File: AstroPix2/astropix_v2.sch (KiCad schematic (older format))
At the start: 41 parts, among them J1 pcie_con, J10 SPI_right, J2 VDD_JP, J3 Vtemp1, J4 SFOut, J5 sample_clock_out, J6 HV_in_external, J7 Conn_01x03, J8 Conn_01x03, J9 SPI_left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

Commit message: PCB: Updated Astropix2 schematic
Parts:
- removed H3, H4: MountingHole, MountingHole:MountingHole_3.2mm_M3, symbol Mechanical:MountingHole
- removed J7: Conn_01x03, Connector_PinHeader_2.54mm:PinHeader_1x03_P2.54mm_Vertical, symbol Connector_Generic:Conn_01x03
- removed U1, U3: OPA320, Package_TO_SOT_SMD:SOT-23-5, symbol Amplifier_Operational:OPA340NA
- added FID1, FID2: Fiducial, Fiducial:Fiducial_1mm_Mask2mm, symbol Mechanical:Fiducial
- added R11, R12: 1k, Resistor_SMD:R_0603_1608Metric, symbol Device:R
- added R13, R14: NC, Resistor_SMD:R_0603_1608Metric, symbol Device:R
- added U1: TLV333, Package_TO_SOT_SMD:SOT-23-6, symbol Amplifier_Operational:ADA4841-1YRJ
- added U3: OPA320S, Package_TO_SOT_SMD:SOT-23-6, symbol Amplifier_Operational:ADA4841-1YRJ
- C3, C4: value .1uF -> 1nF; footprint Capacitor_SMD:C_0603_1608Metric -> Capacitor_SMD:C_1210_3225Metric
- C5, C6: footprint Capacitor_SMD:C_0603_1608Metric -> Capacitor_SMD:C_1210_3225Metric
- J1: value pcie_con -> pcie_GECCO; symbol astropix:pcie_con -> astropix:pcie_GECCO
- R1, R10: value 1k -> 0
- R2: value 22 -> 47
- renumbered C7 to Cvdd1, C8 to Cvdd2, C13 to Cvdd3, C9 to Cvdda1, C10 to Cvdda2, C11 to Cvdda3
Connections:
- net GND: now also U4.B3 (gnda!), R14.2, U1.2 (V-), U3.2 (V-)
- net Inj: now also J1.A28 (C3_1); no longer J1.A36 (C5_1)
- net SFOut: now also U3.3 (+)
- net VDD: now also R13.1
- net VDDA: now also U4.B37 (vdda_temp), U1.5 (~PD), U1.6 (V+), U3.5 (~PD), U3.6 (V+); no longer R8.2
- net Vtemp1: now also U1.3 (+)
- net hold: now also J1.B23 (FMC_LA18_CC_N); no longer J1.B21 (FMC_LA20_N)
- net interrupt: now also J1.B21 (FMC_LA20_N); no longer J1.B18 (FMC_LA22_P)
- net res_n: now also J1.B22 (FMC_LA18_CC_P); no longer J1.B19 (FMC_LA22_N)
- net sample_clock_N: now also J1.B19 (FMC_LA22_N), R14.1; no longer J1.B17 (FMC_LA24_N)
- net sample_clock_P: now also J1.B18 (FMC_LA22_P), R13.2; no longer J1.B16 (FMC_LA24_P)
- net sample_clock_se_N: now also J1.B17 (FMC_LA24_N)
- net sample_clock_se_P: now also J1.B16 (FMC_LA24_P), R8.2
- net sample_clock_se_in: now also R8.1
- net sc_out: now also J5.1 (In)
- net spi_left_clk: now also J1.A16 (FMC_LA23_P)
- net spi_left_csn: now also J1.A17 (FMC_LA23_N)
- net spi_left_miso0: now also J1.A19 (FMC_LA21_N)
- net spi_left_miso1: now also J1.A18 (FMC_LA21_P), J9.3 (Pin_3); no longer J9.1 (Pin_1)
- net spi_left_mosi: now also J1.A20 (FMC_LA19_P), J9.1 (Pin_1); no longer J9.3 (Pin_3)
- net spi_right_clk: now also J10.1 (Pin_1); no longer J10.4 (Pin_4)
- net spi_right_csn: now also J10.4 (Pin_4); no longer J10.5 (Pin_5)
- net spi_right_miso0: now also J10.3 (Pin_3); no longer J10.2 (Pin_2)
- net spi_right_miso1: now also J10.2 (Pin_2); no longer J10.1 (Pin_1)
- net spi_right_mosi: now also J10.5 (Pin_5); no longer J10.3 (Pin_3)
- net sr_sout: now also J1.A23 (FMC_LA17_CC_N); no longer J5.1 (In)
- net suba: now also R12.2; no longer C3.2, C5.2, R1.1, R10.1, U4.B1 (sub), U4.B2 (subdpads)
- net at R6.2: now also U3.1, U3.4 (-)
- net at R2.2: now also U1.1, U1.4 (-)
- new net: R1.1, R10.1, R11.1, R12.1
- new net subd: C3.2, C5.2, R11.2, U4.B1 (sub), U4.B2 (subdpads)
- no-connect marks 58 -> 63
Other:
- note added: "100 Ohm Term + opt. Failsafe"
- note added: "PCB compatible to:\nOPA320S SOT-23-6\nOPA320 SOT-23-5 \n"
- moved on the sheet: C1, C12, C2, C3, C4, C5, C6, J10, J3, J4, J5, J8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

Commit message: PCB: Updated AstroPix2 Schematic
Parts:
- removed J2: VDD_JP, Connector_PinHeader_2.54mm:PinHeader_1x03_P2.54mm_Vertical, symbol Connector_Generic:Conn_01x03
- removed R10: 0, Resistor_SMD:R_0603_1608Metric, symbol Device:R
- added JP1: VDD_JP, Connector_PinHeader_2.54mm:PinHeader_1x03_P2.54mm_Vertical, symbol Jumper:Jumper_3_Bridged12
- added Logo1: KIT_logo, astropix:logo, symbol astropix:KIT_logo
- added R15: 1k, Resistor_SMD:R_0603_1608Metric, symbol Device:R
- added R16: 2k, Resistor_SMD:R_0603_1608Metric, symbol Device:R
- J8: value Conn_01x03 -> VBias
- R1: footprint Resistor_SMD:R_0603_1608Metric -> Resistor_SMD:R_1206_3216Metric
- R9: value 10k -> 680
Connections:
- net GND: now also U4.B17 (sr_RB), R15.2; no longer R9.2
- net POW4_in: now also JP1.3 (B)
- net VDD: now also JP1.2 (C)
- net VDD18_in: now also JP1.1 (A)
- net Vtemp1: now also R9.2; no longer U1.3 (+)
- net pamp: now reaches J8.1 (Pin_1), U4.B25 (pamp)
- net VPBias: now reaches J8.2 (Pin_2), U4.B24 (VPBias)
- net at R2.2, U1.1: now also R16.2; no longer U1.4 (-)
- net at R1.1, R11.1, R12.1: now also J6.1 (In)
- net sr_rb: no longer names the net of R9.1
- net sr_rb: now also U1.3 (+); no longer U4.B17 (sr_RB)
- net sr_sout: no longer names the net of J1.A23 (FMC_LA17_CC_N)
- net sr_sout: no longer U4.B18 (sr_SOUT)
- new net: R15.1, R16.1, U1.4 (-)
- no-connect marks 63 -> 65
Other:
- note added: "100 Ohm Term\nopt. Failsafe R13=2k R14=4k"
- note added: "Configcard"
- note added: "GECCO HV Clearance?\n"
- note added: "Injectioncard"
- note added: "Remove?"
- note added: "Voltagecard"
- note removed: "100 Ohm Term + opt. Failsafe"
- moved on the sheet: C1, C3, C4, C5, C6, Cvdd2, Cvdd3, Cvdda2, Cvdda3, FID1, FID2, J1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

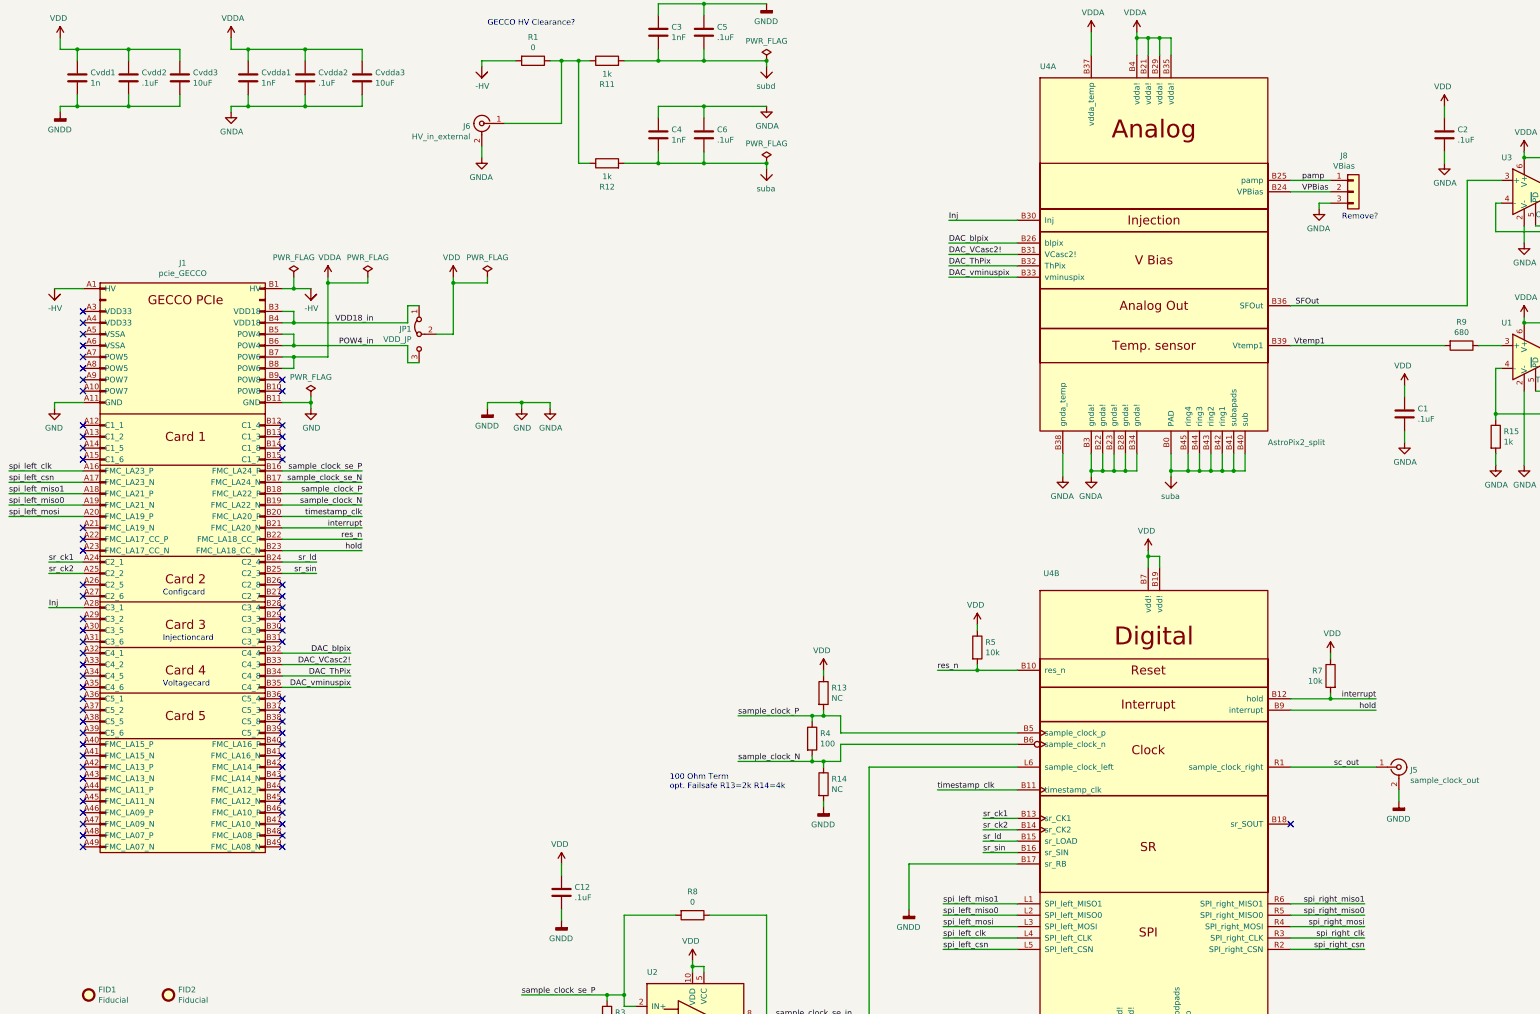
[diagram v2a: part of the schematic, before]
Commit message: Updated Schematic and Asic footprint
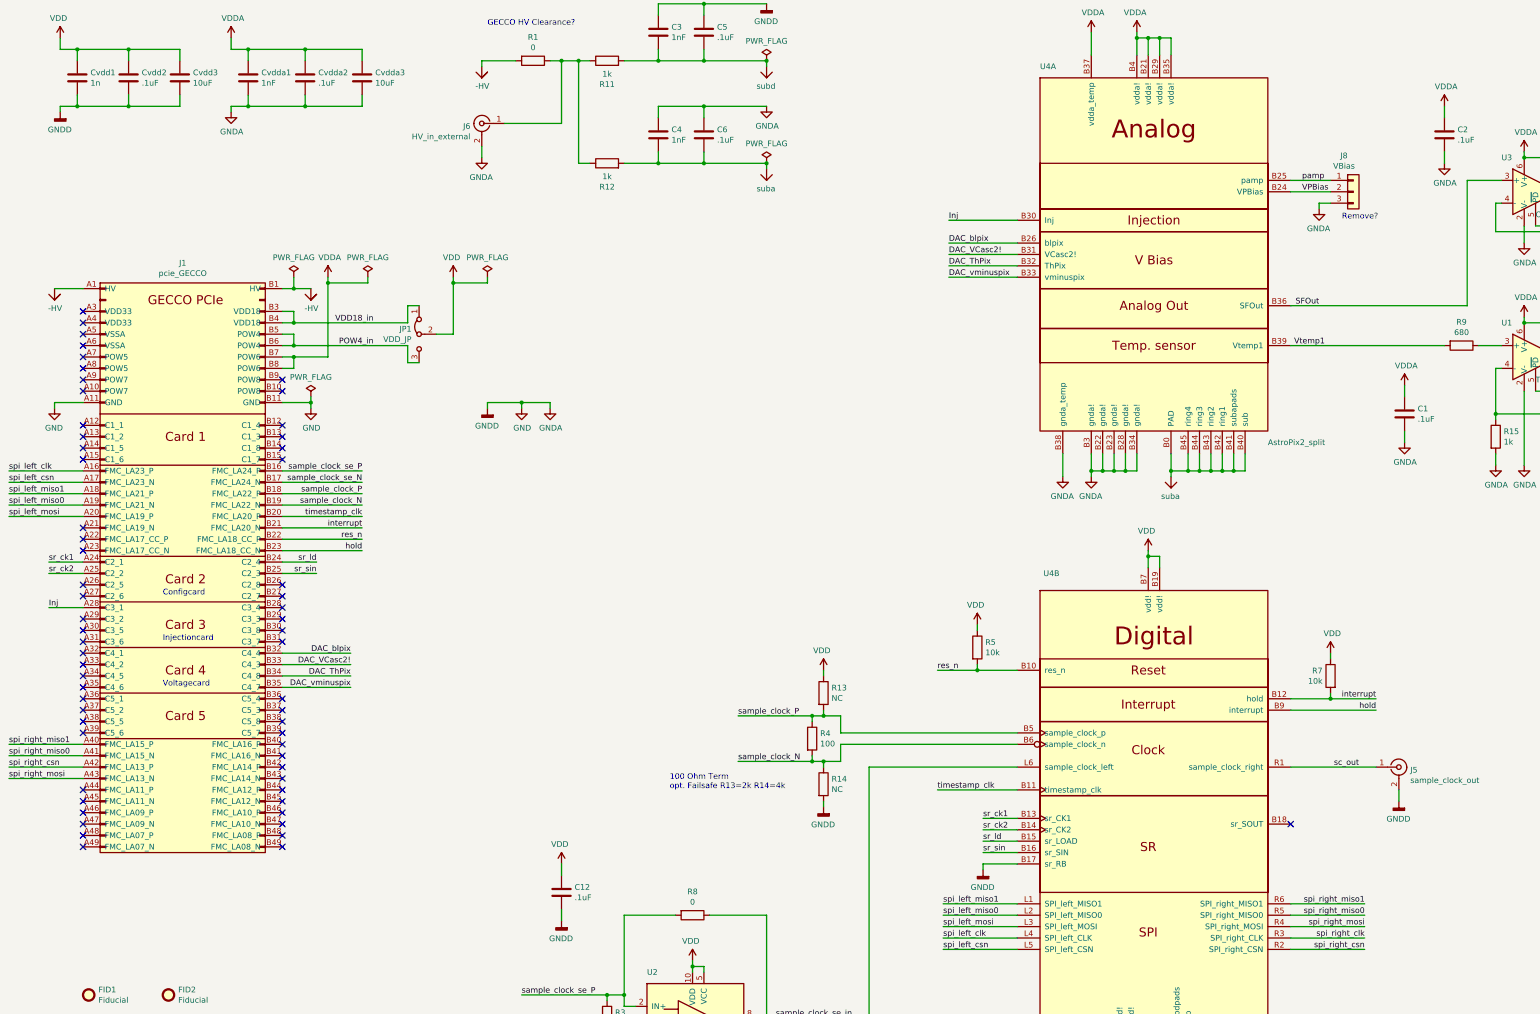
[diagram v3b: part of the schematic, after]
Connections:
- net VDD: no longer C1.1, C2.1
- net VDDA: now also C1.1, C2.1
- net spi_right_csn: now also J1.A42 (FMC_LA13_P)
- net spi_right_miso0: now also J1.A41 (FMC_LA15_N)
- net spi_right_miso1: now also J1.A40 (FMC_LA15_P)
- net spi_right_mosi: now also J1.A43 (FMC_LA13_N)
- no-connect marks 65 -> 61
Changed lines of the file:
@@
 	6050 9700 6050 9750
-$Comp
-L astropix:pcie_GECCO J1
-U 1 1 61228AD2
-P 2350 5400
-F 0 "J1" H 2325 7875 50  0000 C CNN
-F 1 "pcie_GECCO" H 2325 7784 50  0000 C CNN
-F 2 "astropix:pcie_astropix" H 2950 5400 50  0001 C CNN
-F 3 "" H 2950 5400 50  0001 C CNN
-	1    2350 5400
-	1    0    0    -1
-$EndComp
 $Comp
 L Device:C Cvdd1
@@
 Wire Wire Line
 	3800 6350 3200 6350
-NoConn ~ 3200 7150
-NoConn ~ 3200 7250
-NoConn ~ 3200 7350
-NoConn ~ 3200 7450
 NoConn ~ 3200 7550
 NoConn ~ 3200 7650
@@
 NoConn ~ 1450 7650
 NoConn ~ 1450 7550
-NoConn ~ 1450 7450
-NoConn ~ 1450 7350
-NoConn ~ 1450 7250
-NoConn ~ 1450 7150
 NoConn ~ 1450 6050
 NoConn ~ 1450 6150
@@
 Wire Wire Line
 	3900 5450 3200 5450
-Wire Wire Line
-	8700 8200 9650 8200
-$Comp
-L power:GNDD #PWR0140
-U 1 1 611F5306
-P 8700 8600
-F 0 "#PWR0140" H 8700 8350 50  0001 C CNN
-F 1 "GNDD" H 8704 8445 50  0000 C CNN
-F 2 "" H 8700 8600 50  0001 C CNN
-F 3 "" H 8700 8600 50  0001 C CNN
-	1    8700 8600
-	-1   0    0    -1
-$EndComp
 NoConn ~ 1450 5750
 NoConn ~ 1450 5850
@@
 Connection ~ 6900 650
 $Comp
-L power:VDD #PWR0148
-U 1 1 6120E196
-P 13050 4000
-F 0 "#PWR0148" H 13050 3850 50  0001 C CNN
-F 1 "VDD" H 13065 4173 50  0000 C CNN
-F 2 "" H 13050 4000 50  0001 C CNN
-F 3 "" H 13050 4000 50  0001 C CNN
-	1    13050 4000
-	-1   0    0    -1
-$EndComp
-$Comp
 L Device:C C1
 U 1 1 6120E19C
@@
 	13900 2200 13600 2200
 $Comp
-L power:VDD #PWR0146
-U 1 1 611F9AB5
-P 13400 1550
-F 0 "#PWR0146" H 13400 1400 50  0001 C CNN
-F 1 "VDD" H 13415 1723 50  0000 C CNN
-F 2 "" H 13400 1550 50  0001 C CNN
-F 3 "" H 13400 1550 50  0001 C CNN
-	1    13400 1550
-	-1   0    0    -1
-$EndComp
-$Comp
 L Device:C C2
 U 1 1 611F9ABB
@@
 Text Label 12150 2300 0    50   ~ 0
 VPBias
-Wire Wire Line
-	8700 8200 8700 8600
 $Comp
 L astropix:KIT_logo Logo1
@@
 Text Notes 5000 850  0    50   ~ 0
 GECCO HV Clearance?\n
+$Comp
+L power:GNDD #PWR0140
+U 1 1 611F5306
+P 9350 8250
+F 0 "#PWR0140" H 9350 8000 50  0001 C CNN
+F 1 "GNDD" H 9354 8095 50  0000 C CNN
+F 2 "" H 9350 8250 50  0001 C CNN
+F 3 "" H 9350 8250 50  0001 C CNN
+	1    9350 8250
+	-1   0    0    -1
+$EndComp
+Wire Wire Line
+	9350 8250 9350 8200
+Wire Wire Line
+	9350 8200 9650 8200
+$Comp
+L astropix:pcie_GECCO J1
+U 1 1 61228AD2
+P 2350 5400
+F 0 "J1" H 2325 7875 50  0000 C CNN
+F 1 "pcie_GECCO" H 2325 7784 50  0000 C CNN
+F 2 "astropix:pcie_astropix" H 2950 5400 50  0001 C CNN
+F 3 "" H 2950 5400 50  0001 C CNN
+	1    2350 5400
+	1    0    0    -1
+$EndComp
+NoConn ~ 3200 7450
+NoConn ~ 3200 7350
+NoConn ~ 3200 7250
+NoConn ~ 3200 7150
+Wire Wire Line
+	800  7450 1450 7450
+Wire Wire Line
+	800  7350 1450 7350
+Wire Wire Line
+	800  7250 1450 7250
+Wire Wire Line
+	800  7150 1450 7150
+Text Label 800  7450 0    50   ~ 0
+spi_right_mosi
+Text Label 800  7250 0    50   ~ 0
+spi_right_miso0
+Text Label 800  7350 0    50   ~ 0
+spi_right_csn
+Text Label 800  7150 0    50   ~ 0
+spi_right_miso1
+$Comp
+L power:VDDA #PWR?
+U 1 1 61134A9E
+P 13400 1550
+F 0 "#PWR?" H 13400 1400 50  0001 C CNN
+F 1 "VDDA" H 13415 1723 50  0000 C CNN
+F 2 "" H 13400 1550 50  0001 C CNN
+F 3 "" H 13400 1550 50  0001 C CNN
+	1    13400 1550
+	1    0    0    -1
+$EndComp
+$Comp
+L power:VDDA #PWR?
+U 1 1 6114F02E
+P 13050 4000
+F 0 "#PWR?" H 13050 3850 50  0001 C CNN
+F 1 "VDDA" H 13065 4173 50  0000 C CNN
+F 2 "" H 13050 4000 50  0001 C CNN
+F 3 "" H 13050 4000 50  0001 C CNN
+	1    13050 4000
+	1    0    0    -1
+$EndComp
 $EndSCHEMATC
